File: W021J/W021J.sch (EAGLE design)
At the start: 3 parts, among them X1 FH12-18S-0.5SH, X2 FH12-18S-0.5SH

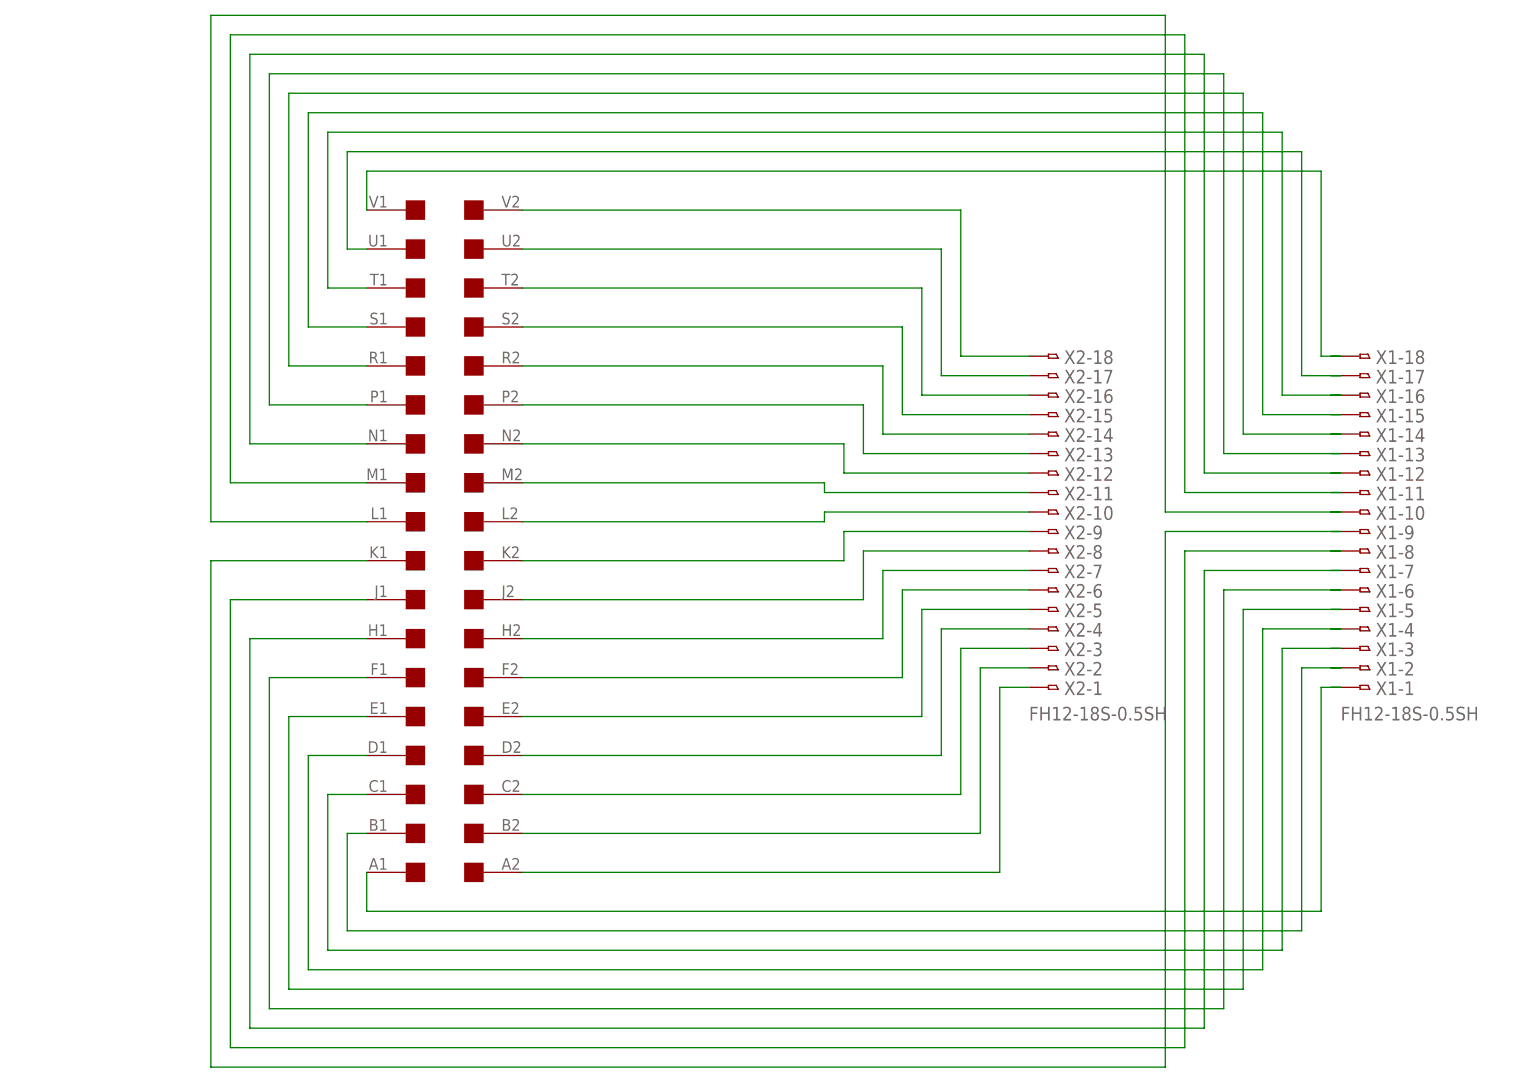
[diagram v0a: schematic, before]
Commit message: Redesigned memory expansion to fit on a single flip chip, consolidated component libraries, etc.
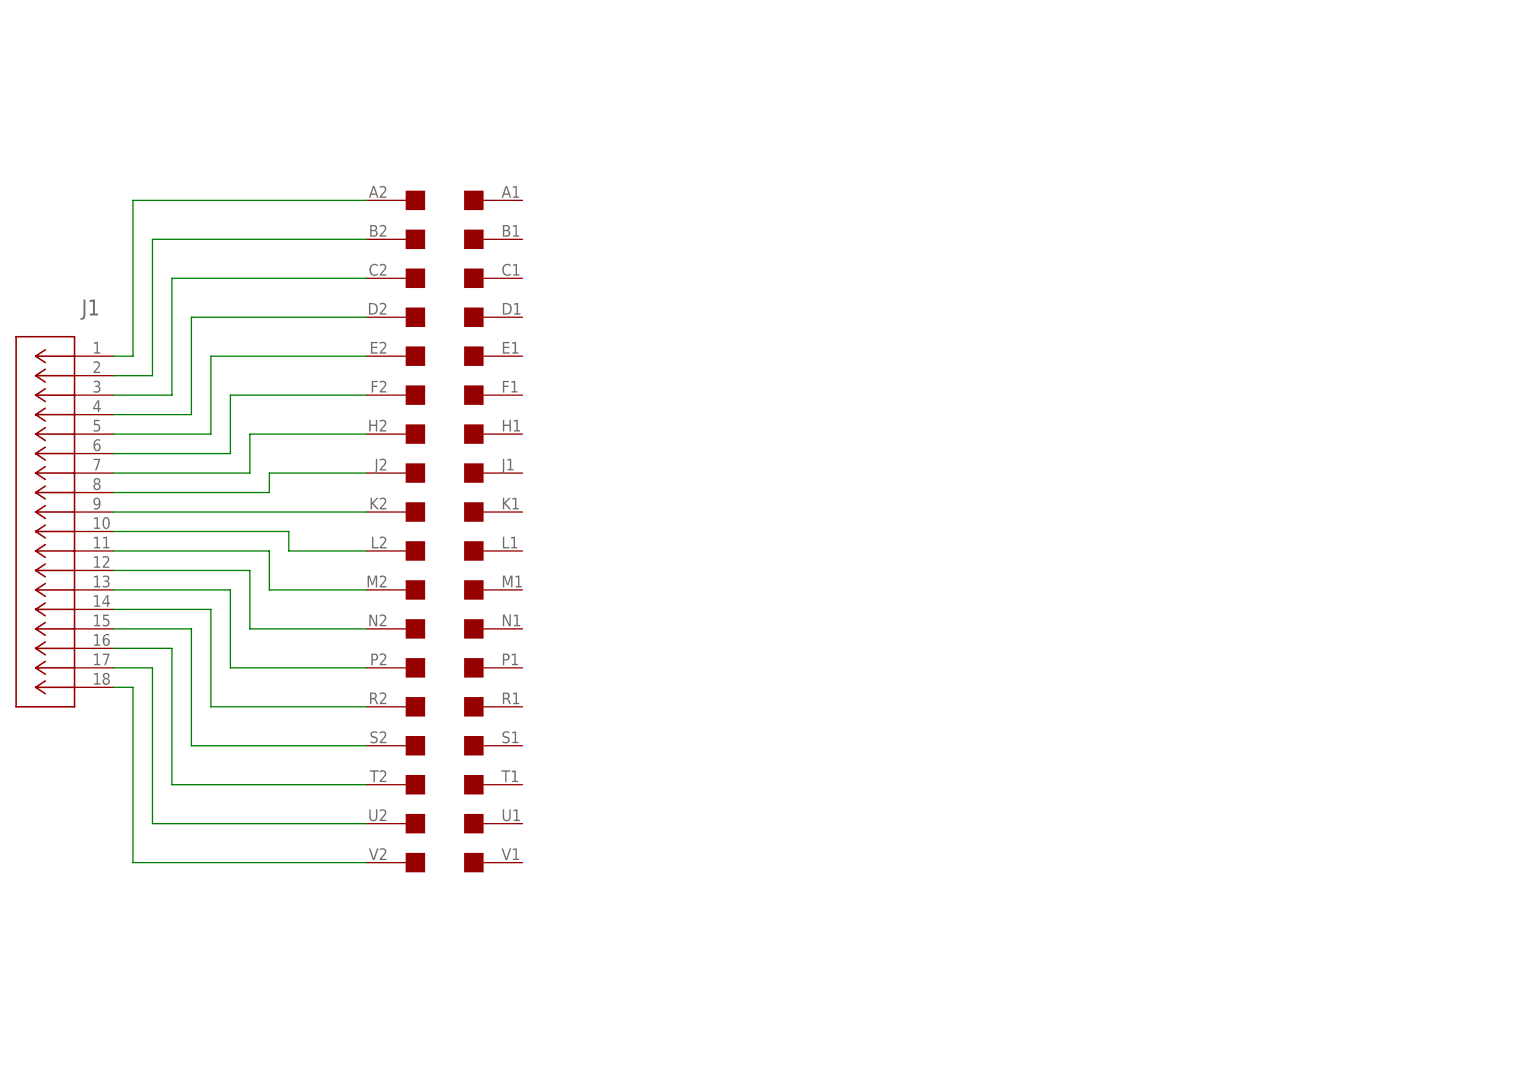
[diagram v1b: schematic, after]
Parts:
- removed X1, X2: FH12-18S-0.5SH, con-hirose:FH12-18S-0.5SH
- added J1: 503480-1800, MM24I:503480-1800
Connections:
- removed net N$19: EDGE1V1.1, X1-18.1
- removed net N$20: EDGE1U1.1, X1-17.1
- removed net N$21: EDGE1T1.1, X1-16.1
- removed net N$23: EDGE1R1.1, X1-14.1
- removed net N$25: EDGE1N1.1, X1-12.1
- removed net N$27: EDGE1L1.1, X1-10.1
- removed net N$32: EDGE1D1.1, X1-4.1
- removed net N$33: EDGE1E1.1, X1-5.1
- removed net N$34: EDGE1F1.1, X1-6.1
- removed net N$37: EDGE1A2.1, X2-1.1
- removed net N$39: EDGE1M1.1, X1-11.1
- removed net N$41: EDGE1S1.1, X1-15.1
- removed net N$43: EDGE1P1.1, X1-13.1
- removed net N$44: EDGE1A1.1
- removed net N$45: EDGE1K1.1, X1-9.1
- removed net N$46: EDGE1B1.1
- removed net N$47: EDGE1J1.1, X1-8.1
- removed net N$48: EDGE1H1.1, X1-7.1
- removed net N$52: EDGE1C1.1, X1-3.1
- removed net N$53: X1-2.1
- removed net N$54: X1-1.1
- new net N$18: EDGE1F2.1, J1.6
- net N$1: now also EDGE1A2.1, J1.1; no longer EDGE1V2.1, X2-18.1
- net N$10: now also EDGE1P2.1, J1.13; no longer EDGE1K2.1, X2-9.1
- net N$11: now also EDGE1N2.1, J1.12; no longer EDGE1J2.1, X2-8.1
- net N$12: now also EDGE1M2.1, J1.11; no longer EDGE1H2.1, X2-7.1
- net N$13: now also EDGE1L2.1, J1.10; no longer EDGE1F2.1, X2-6.1
- net N$14: now also EDGE1K2.1, J1.9; no longer EDGE1E2.1, X2-5.1
- net N$15: now also EDGE1J2.1, J1.8; no longer EDGE1D2.1, X2-4.1
- net N$16: now also EDGE1H2.1, J1.7; no longer EDGE1C2.1, X2-3.1
- net N$17: now also EDGE1E2.1, J1.5; no longer EDGE1B2.1, X2-2.1
- net N$2: now also EDGE1B2.1, J1.2; no longer EDGE1U2.1, X2-17.1
- net N$3: now also EDGE1C2.1, J1.3; no longer EDGE1T2.1, X2-16.1
- net N$4: now also EDGE1D2.1, J1.4; no longer EDGE1S2.1, X2-15.1
- net N$5: now also EDGE1V2.1, J1.18; no longer EDGE1R2.1, X2-14.1
- net N$6: now also EDGE1U2.1, J1.17; no longer EDGE1P2.1, X2-13.1
- net N$7: now also EDGE1T2.1, J1.16; no longer EDGE1N2.1, X2-12.1
- net N$8: now also EDGE1S2.1, J1.15; no longer EDGE1M2.1, X2-11.1
- net N$9: now also EDGE1R2.1, J1.14; no longer EDGE1L2.1, X2-10.1
